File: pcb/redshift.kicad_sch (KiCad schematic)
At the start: 74 parts, among them IC1 LPC5526JEV98, J1 USB_C_Receptacle_USB2.0, J2 Side, J3 Conn_01x06_Female, SW1 SW_SP, SW2 SW_SP, SW3 SW_SP, U1 PAW3399DM‐T4QU, U3 TCR2LE19,LM(CT, U4 MIC5528-3.3YMT-TR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

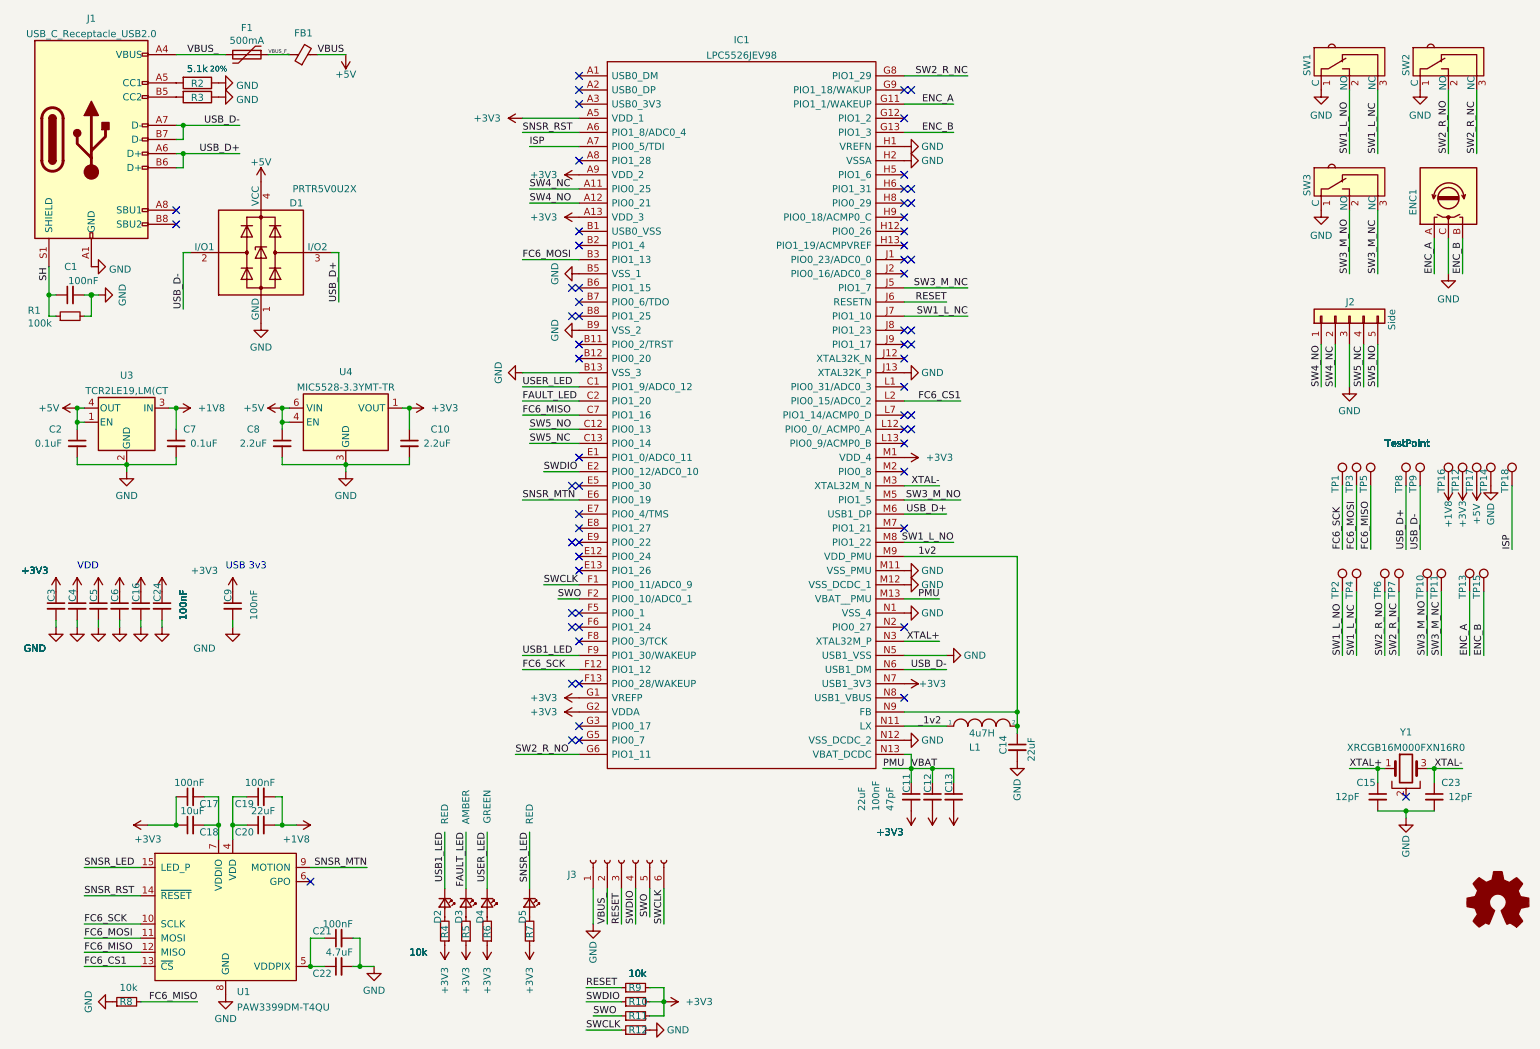
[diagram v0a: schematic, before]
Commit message: Debug fixes
- add 10 pin debug connector
- remove uneeded pull up resistors on pins (MCU has internal ones)
- add a diode to protect reverse current on the debug pins
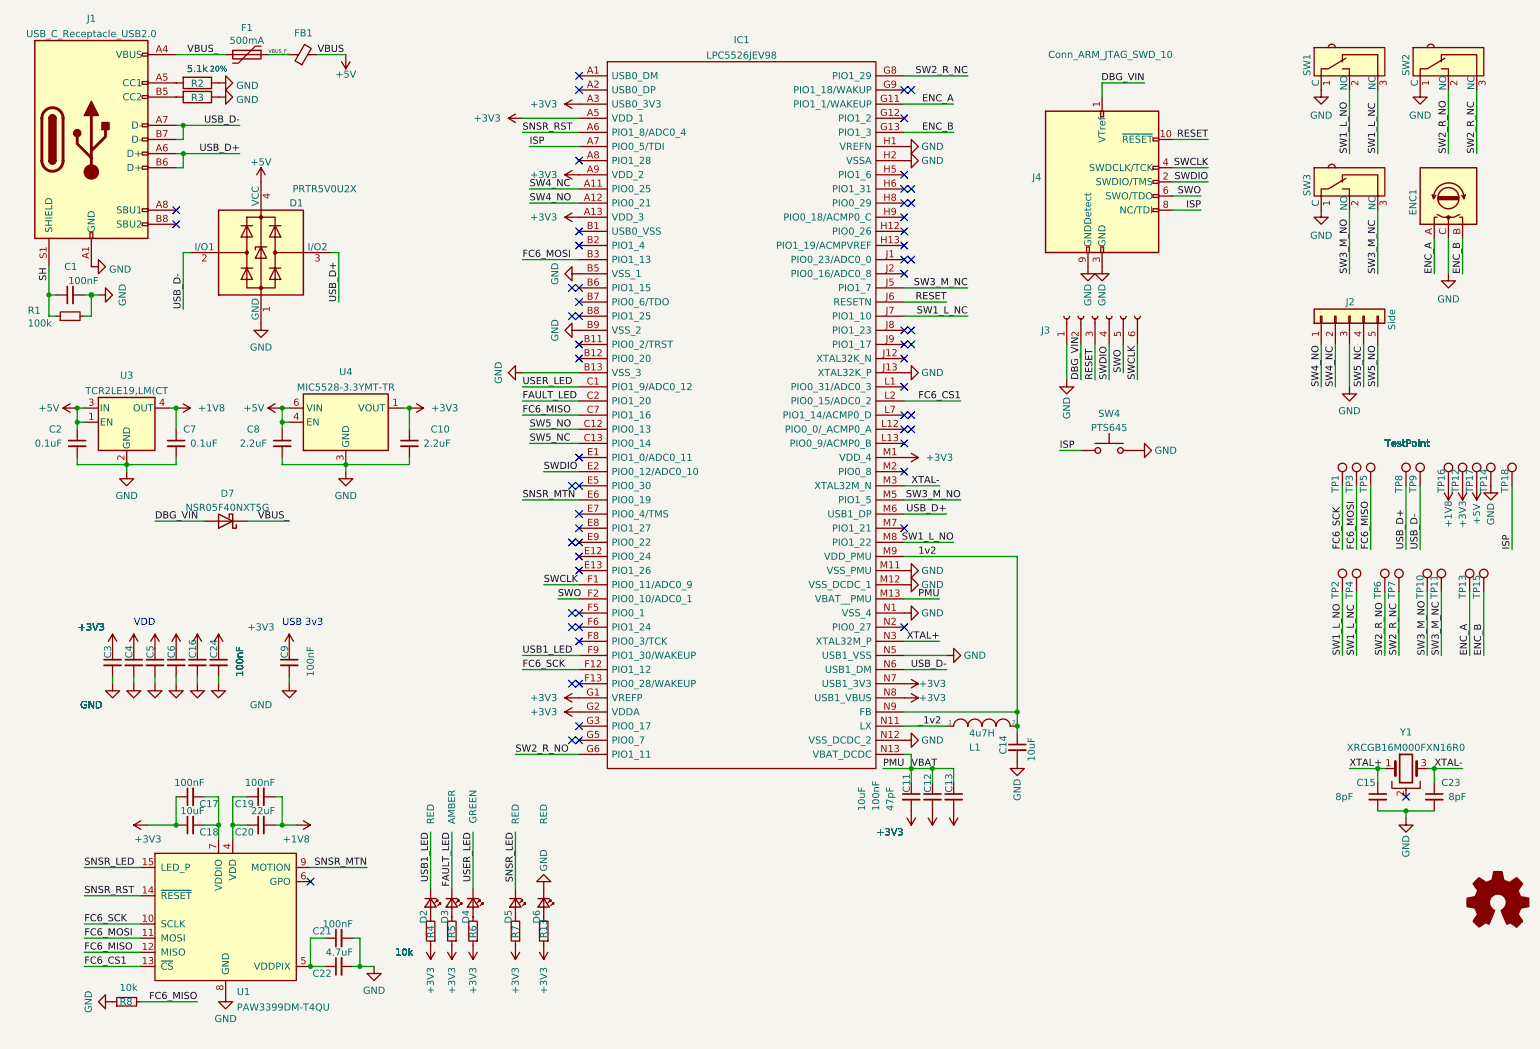
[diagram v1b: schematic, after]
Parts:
- removed R10, R11, R12, R9: 10k, Resistor_SMD:R_0402_1005Metric, symbol Device:R_Small
- added D6: RED, LED_SMD:LED_0402_1005Metric, symbol Device:LED_Small
- added D7: NSR05F40NXT5G, Diode_SMD:D_0402_1005Metric, symbol Device:D_Schottky
- added J4: Conn_ARM_JTAG_SWD_10, Connector_PinHeader_1.27mm:PinHeader_2x05_P1.27mm_Vertical_SMD, symbol Connector:Conn_ARM_JTAG_SWD_10
- added R13: 10k, Resistor_SMD:R_0402_1005Metric, symbol Device:R_Small
- added SW4: PTS645, Button_Switch_SMD:SW_SPST_PTS645, symbol Switch:SW_Push
- C11, C14: value 22uF -> 10uF
- C15, C23: value 12pF -> 8pF
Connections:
- net +1V8: now also U3.4 (OUT); no longer U3.3 (IN)
- net +3V3: now also IC1.A3 (USB0_3V3), IC1.N8 (USB1_VBUS), R13.1
- net +5V: now also U3.3 (IN); no longer U3.4 (OUT)
- net GND: now also D6.1 (K), J4.3 (GND), J4.5 (GND), J4.9 (GNDDetect), SW4.2
- net ISP: now also J4.8 (NC/TDI), SW4.1
- net RESET: now also J4.10 (~{RESET})
- net SWCLK: now also J4.4 (SWDCLK/TCK)
- net SWDIO: now also J4.2 (SWDIO/TMS)
- net SWO: now also J4.6 (SWO/TDO)
- net VBUS_: now also D7.1 (K); no longer J3.2 (Pin_2)
- new net: D6.2 (A), R13.2
- new net DBG_VIN: D7.2 (A), J3.2 (Pin_2), J4.1 (VTref)
- no-connect marks 65 -> 63
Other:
- moved on the sheet: C16, C24, C3, C4, C5, C6, C9, D2, D3, D4, D5, J3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

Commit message: bump version, use proper spec Caps
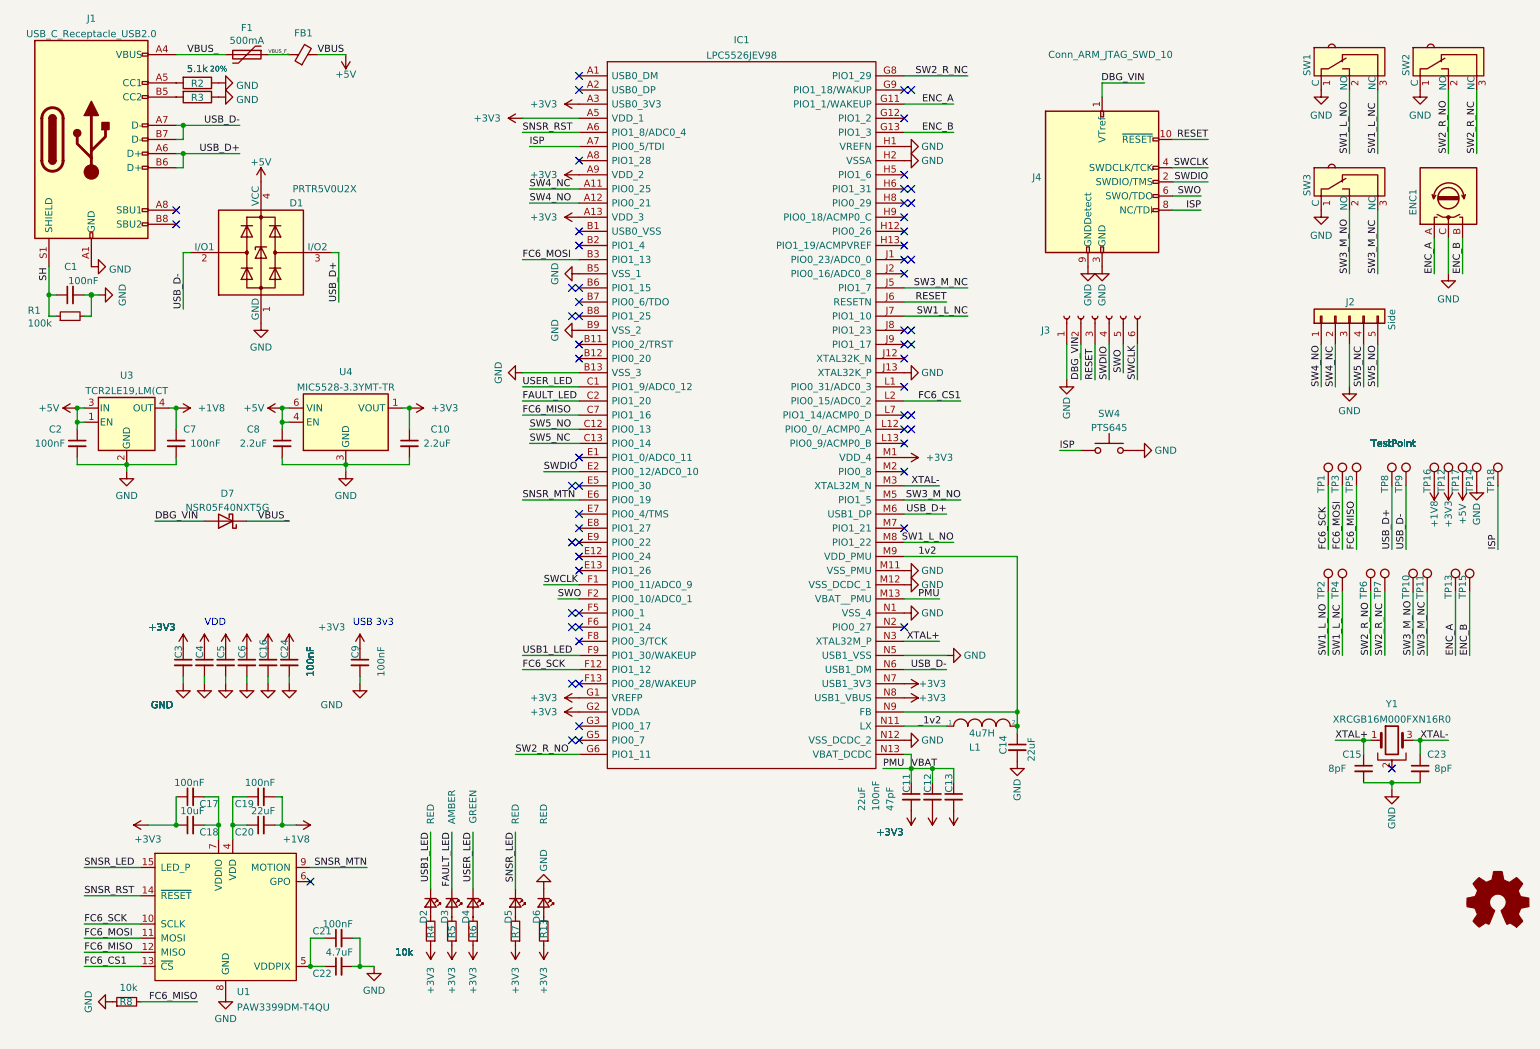
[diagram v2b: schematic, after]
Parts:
- C11, C14: value 10uF -> 22uF
- C2, C7: value 0.1uF -> 100nF
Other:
- moved on the sheet: C15, C16, C23, C24, C3, C4, C5, C6, C9, TP1, TP10, TP11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
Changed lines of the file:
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@@
     (title "Redshift")
     (date "2021-12-22")
-    (rev "0.1")
+    (rev "0.2")
     (company "Dekanova LLC                                       https://github.com/Dekanova/redshift")
     (comment 3 "This source describes Open Hardware and is licensed under the CERN-OHL-Rv2")

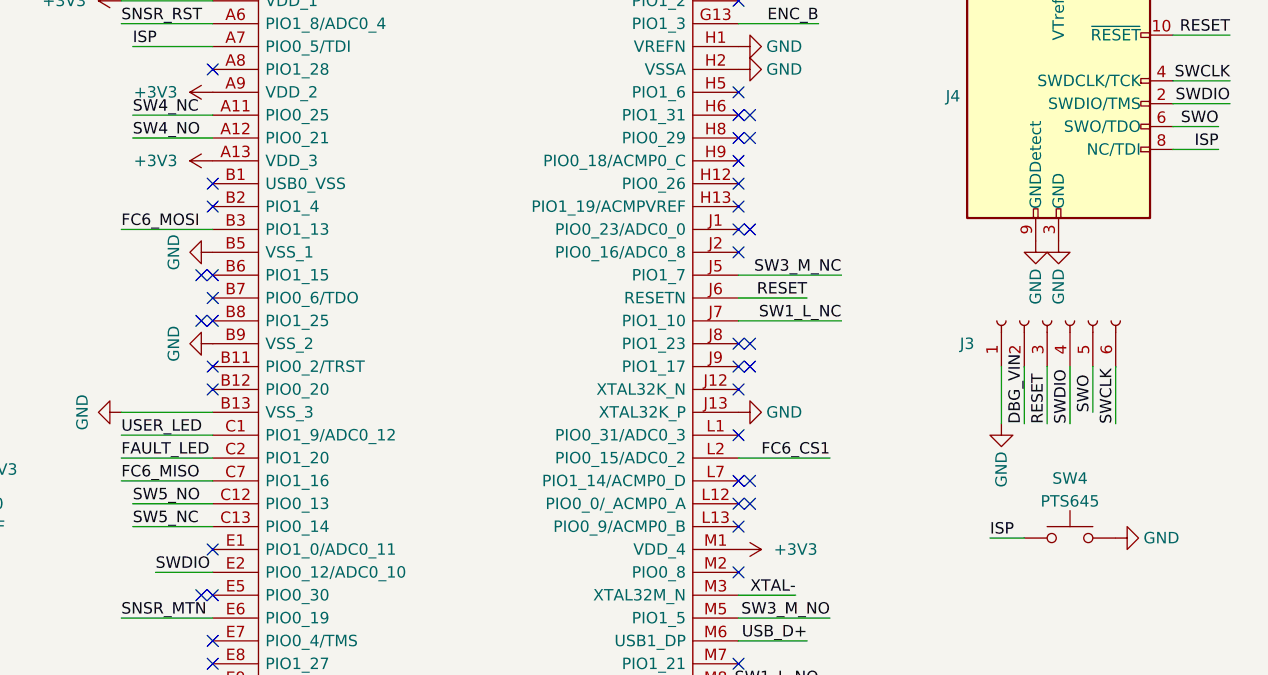
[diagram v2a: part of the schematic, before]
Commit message: ground unused USB line per datasheet, use smaller switch for ISP
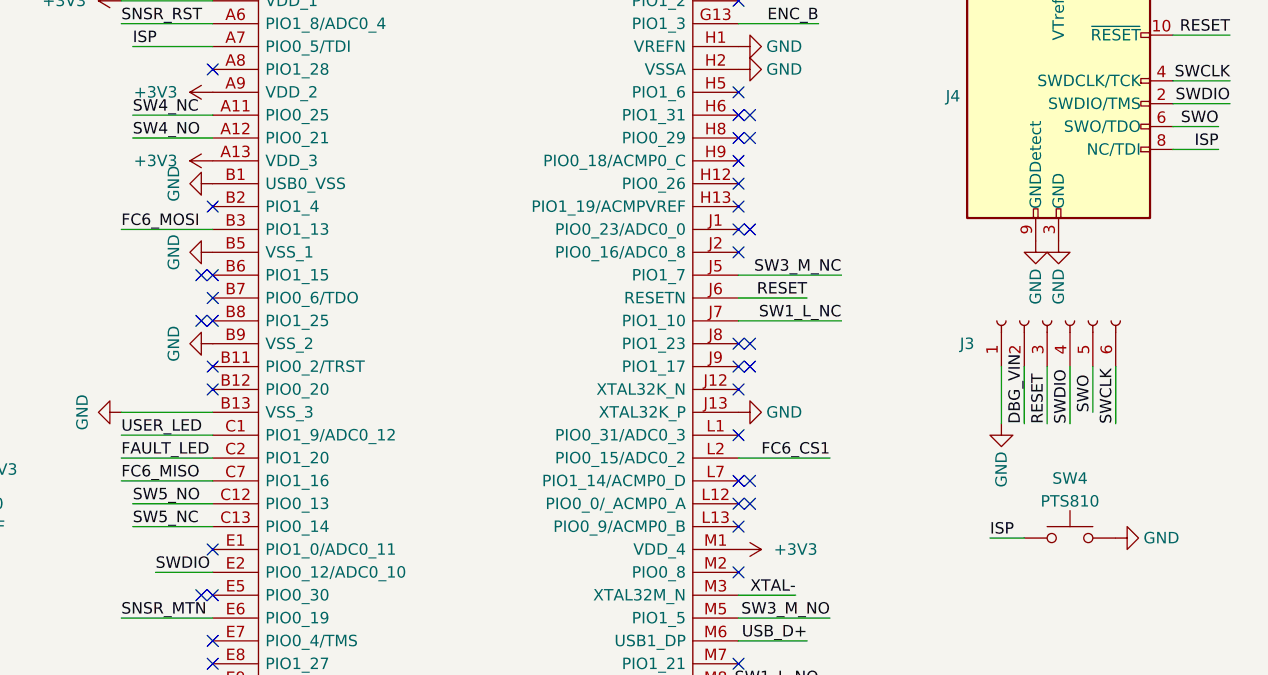
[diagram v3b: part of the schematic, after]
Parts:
- J4: now left out of the parts list
- SW4: value PTS645 -> PTS810; footprint Button_Switch_SMD:SW_SPST_PTS645 -> Button_Switch_SMD:SW_SPST_PTS810
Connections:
- net GND: now also IC1.B1 (USB0_VSS)
- no-connect marks 63 -> 62

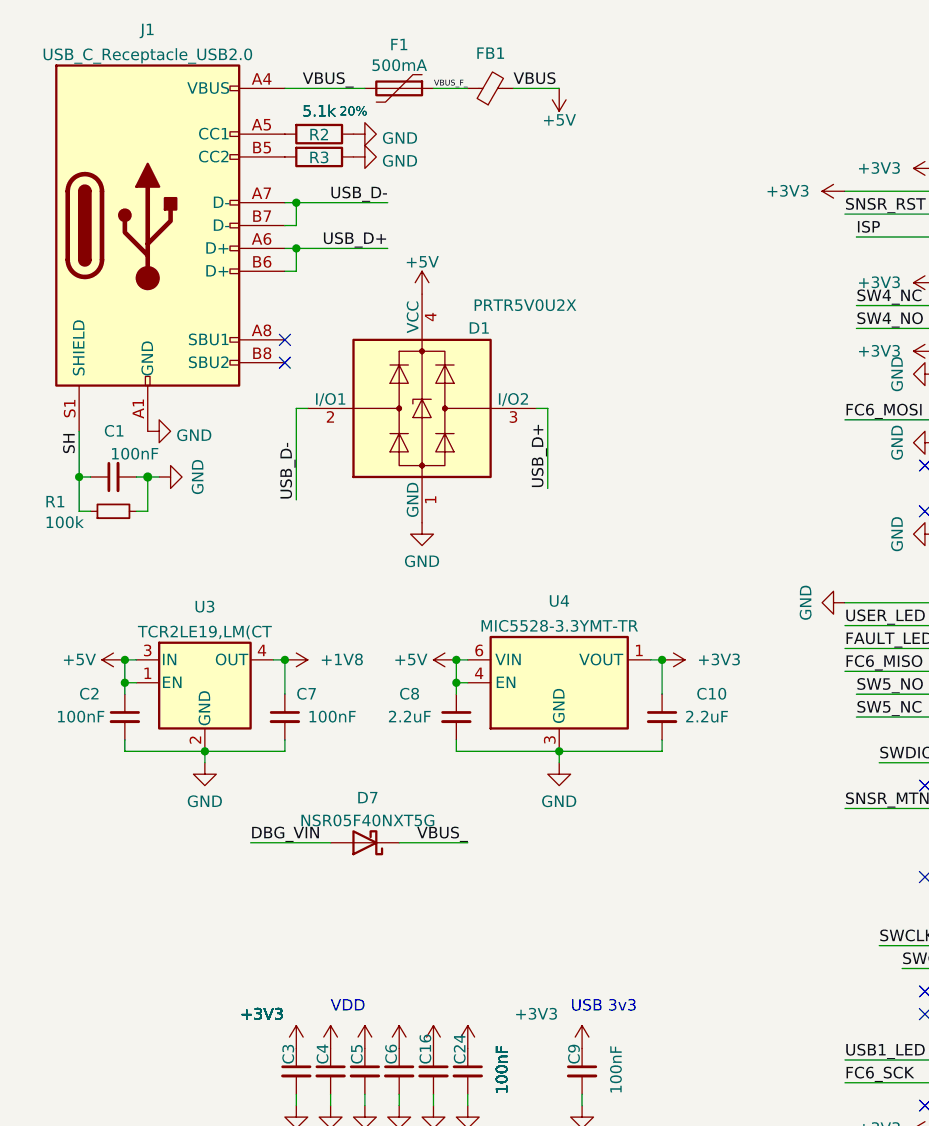
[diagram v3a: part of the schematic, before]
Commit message: Replaced Old LDO
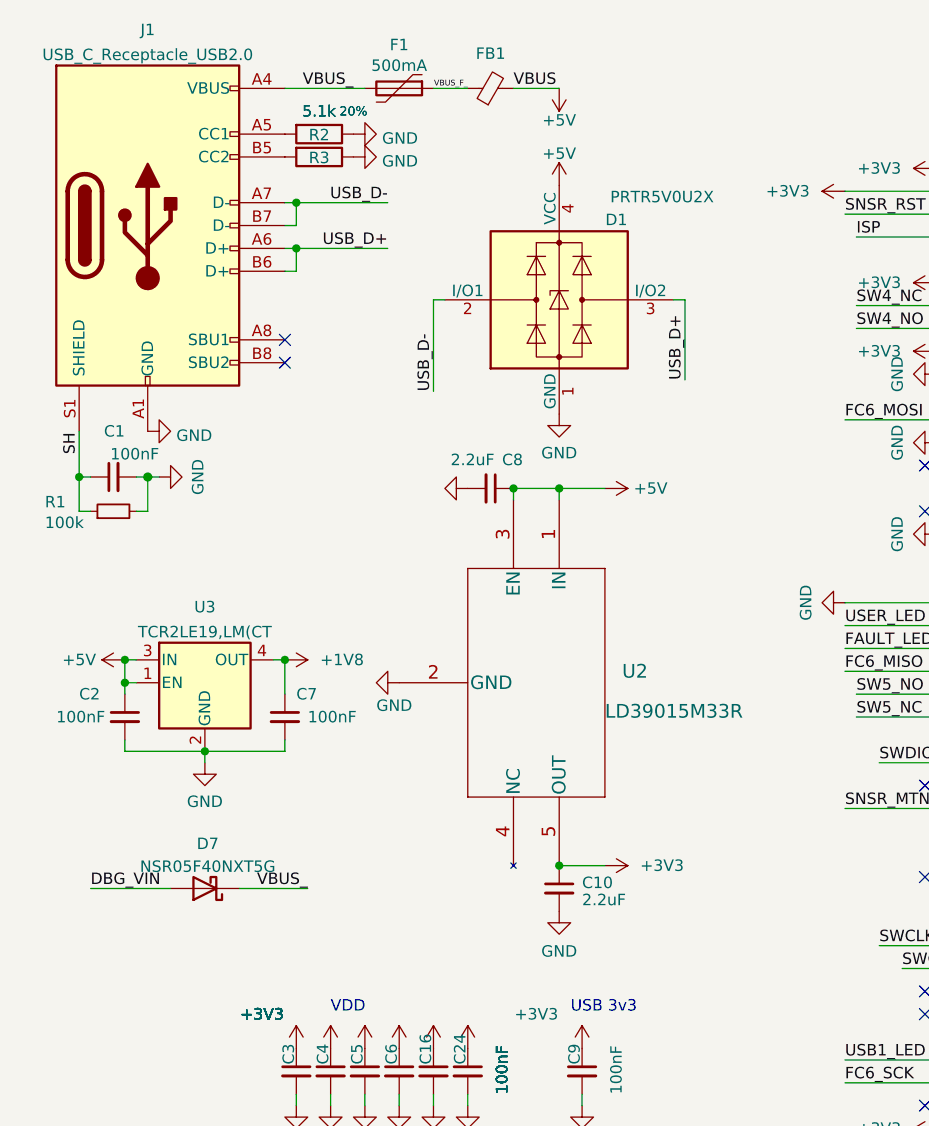
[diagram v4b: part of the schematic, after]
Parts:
- removed U4: MIC5528-3.3YMT-TR, MIC5528-3:SON40P120X120X60-7N, symbol Regulator_Linear:MIC5504-3.3YM5
- added U2: LD39015M33R, symbol LD39015M33R:LD39015M33R
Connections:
- net +3V3: now also U2.5 (OUT)
- net +5V: now also U2.1 (IN), U2.3 (EN)
- net GND: now also U2.2 (GND)
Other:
- moved on the sheet: C8, D1, D7
